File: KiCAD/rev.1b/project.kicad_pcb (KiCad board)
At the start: 2 copper layers, 23.9 x 26 mm, 8 parts, among them J1 Conn_01x07, J2 Conn_01x07, J3 Conn_Coaxial, U1 RFM95W

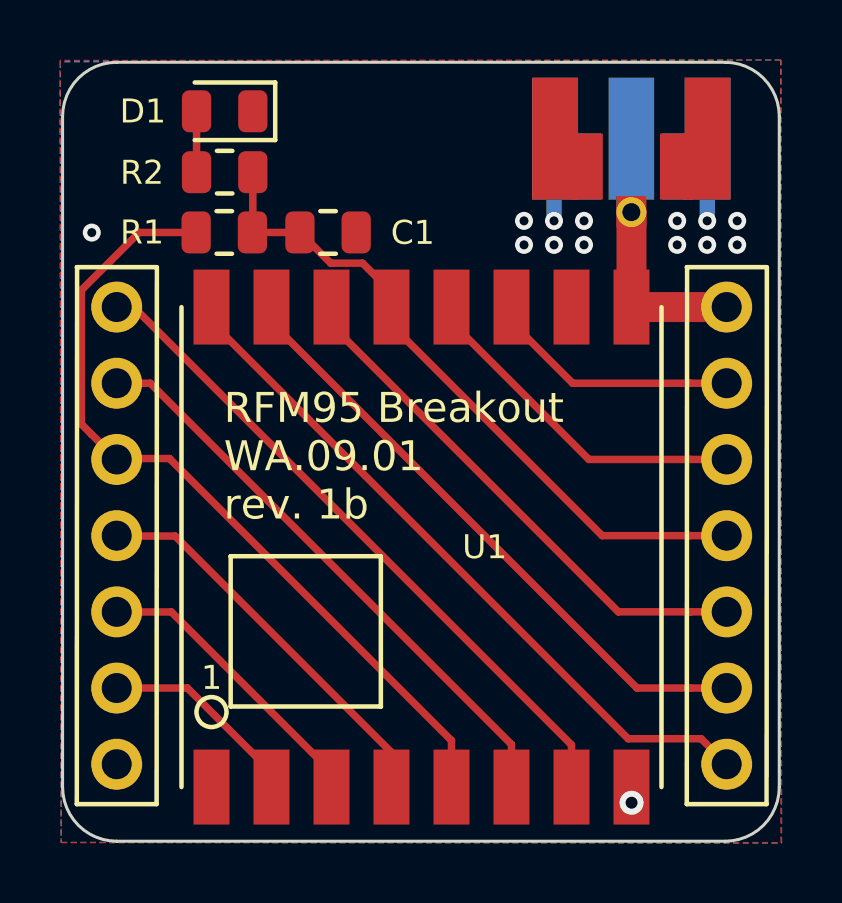
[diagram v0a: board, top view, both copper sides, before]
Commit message: Increase minimum clearances and make suitable for at-home single layer PCB construction.
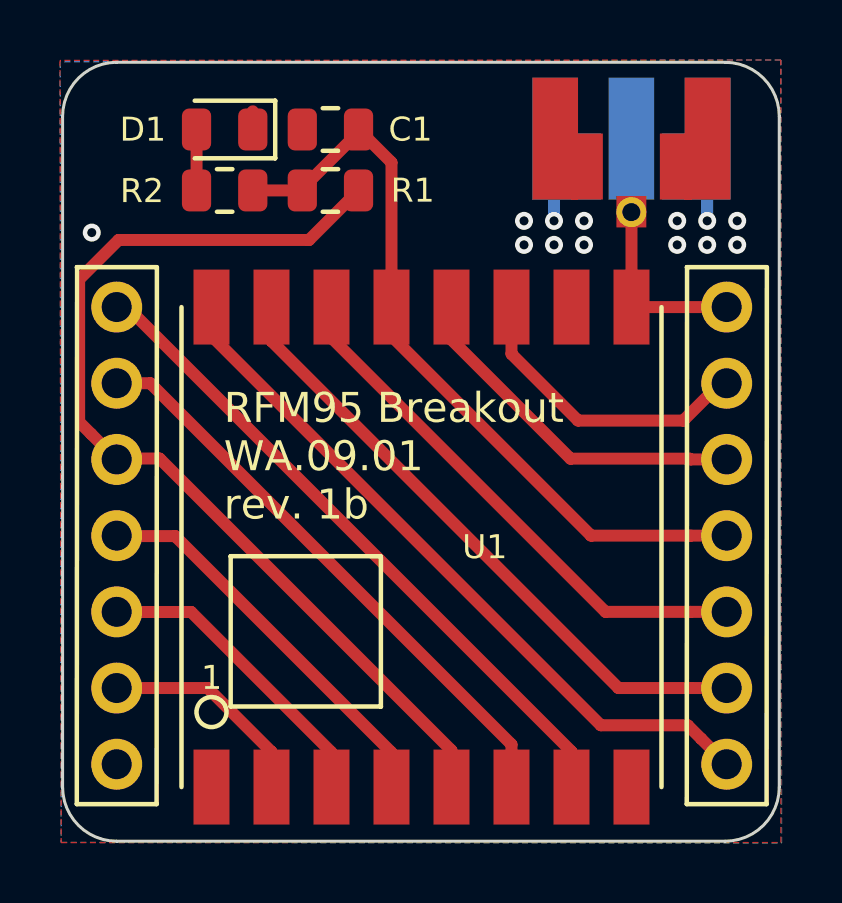
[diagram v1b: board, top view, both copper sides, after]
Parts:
- moved R1 3.80 mm to (125.1, 80.4), turned to 0 degrees
- moved C1 3.43 mm to (125.1, 78.4), turned to 0 degrees
- moved R2 0.61 mm to (121.6, 80.4)
- moved D1 0.61 mm to (121.6, 78.4)
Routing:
- net /NSS: track 27.4 -> 33.4 mm
- net +3V3: track 22.7 -> 25.7 mm
- net /DIO3: track 8.52 -> 10.2 mm
- net GND: vias 14 -> 13
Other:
- net class Default: trace_width 0.25 -> 0.4
- rule trace_min: 0.2 -> 0.4
